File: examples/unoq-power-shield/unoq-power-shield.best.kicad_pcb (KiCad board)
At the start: 4 copper layers, 53.3 x 68.6 mm, 56 parts, among them J1 VIN 7-24V, J10 UNO PWR, J11 UNO ANALOG, J12 UNO D0-D7, J13 UNO D8-SCL, J2 5V OUT, J3 Qwiic, J4 Qwiic, J5 5V IO, Q1 BSS138LT1G, Q2 BSS138LT1G, Q3 BSS138LT1G, Q4 BSS138LT1G, Q5 AO4407A, U1 TPS54331DDAR, U2 INA226AIDGSR

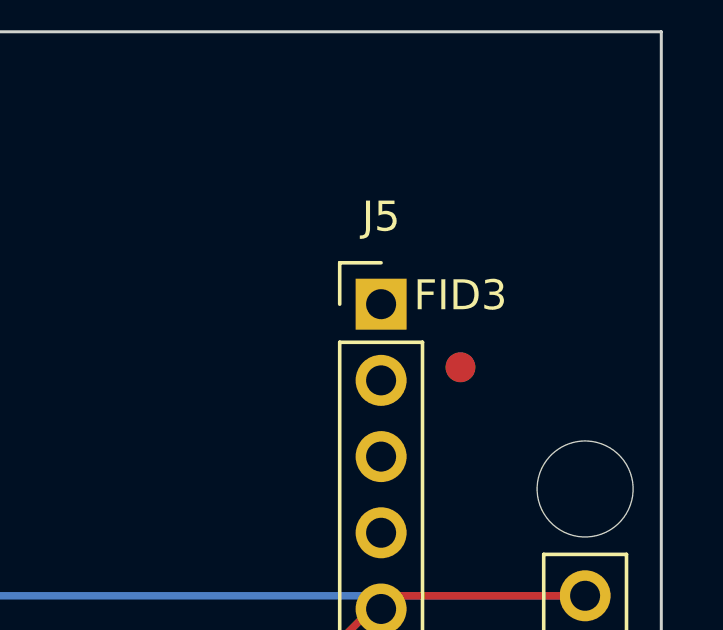
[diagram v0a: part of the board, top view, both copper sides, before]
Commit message: Routing loop closed: xvfb in route.py, DSN sanity, checker interior test
Four measured fixes from driving the example board through route/check:

- route.py wraps freerouting 1.9.0 in xvfb-run when headless (the Xvfb
  decision lived only in the Dockerfile; the invocation still died with
  HeadlessException).
- export_dsn withholds SURFACE pours from the DSN (in-memory only):
  ExportSpecctraDSN writes every zone as a Specctra (plane ...) that
  freerouting treats as fixed copper, so a ground flood on a routable
  layer walls off the whole layer - measured 16 unfinished nets on a
  2-signal-layer board. Plane-layer pours stay: that IS the semantics.
  It also sanitises class names: KiCad 10 exports "Power,Default" and
  the comma splits the Specctra token, so freerouting never bound those
  nets and routed power at the default width - the exact thin-power
  failure the checker flagged.
- validate_gerbers keepout test uses the strict interior (1um epsilon):
  a pour correctly carved around a keepout leaves vertices exactly ON
  the boundary, and flagging those fails every fill that did the right
  thing.
- zones.py fills to a temp file and swaps (kct now refuses -o == input),
  and its fill verification runs in a fresh interpreter (second
  LoadBoard after zone edits returns a bare SwigPyObject).

Example board across these rounds: checker 12->13 passed, antenna
keepout PASS with real carved pours, VIN/VIN_PROT/VIN_RAW at 0.30, DRC
unconnected 6 -> 2, violation kinds stable across all 5 samples.

Co-Authored-By: Claude Fable 5 <noreply@anthropic.com>
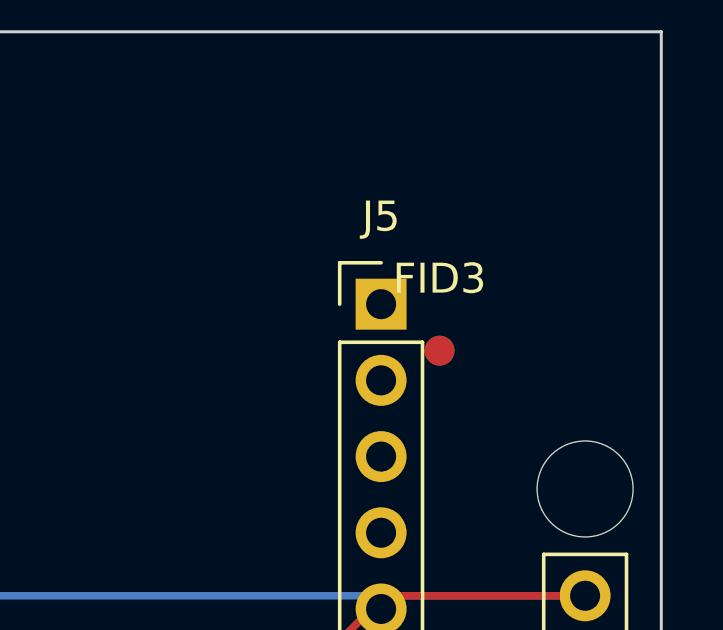
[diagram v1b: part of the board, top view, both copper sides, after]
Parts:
- moved FID3 0.89 mm to (167.8, 81.3)
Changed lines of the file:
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@@
 	(footprint "Fiducial_pcb-agent"
 		(layer "F.Cu")
-		(at 168.4754 81.8927)
+		(at 167.78 81.34)
 		(property "Reference" "FID3"
 			(at -0.001254 -2.39625 0)
